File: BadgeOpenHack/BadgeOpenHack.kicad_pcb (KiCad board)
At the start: 2 copper layers, 38.1 x 48.2 mm, 27 parts, among them J1 Conn_01x04_Male, J2 USB_B_Micro, SW1 RST, U1 ATSAMD11C14A-SS, U2 AP2112K-3.3

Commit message: remove logos inncesary
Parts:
- removed the G*** at (180.0, 101.0)
- removed the G*** at (189.5, 95.5)

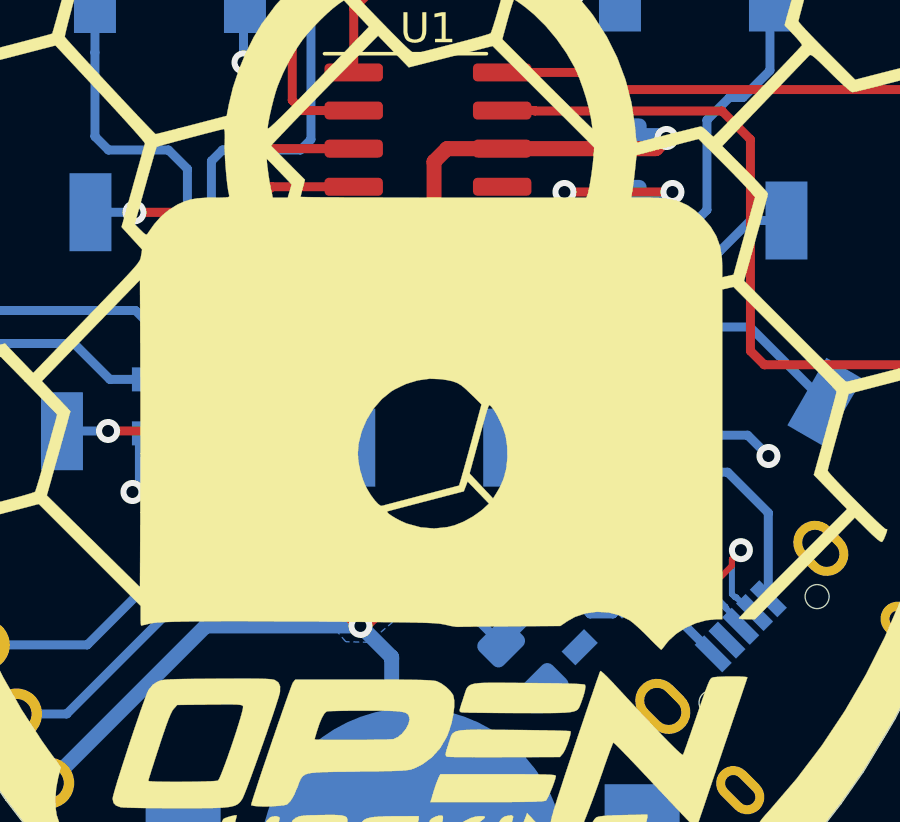
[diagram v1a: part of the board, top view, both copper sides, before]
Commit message: Fix logos and vias
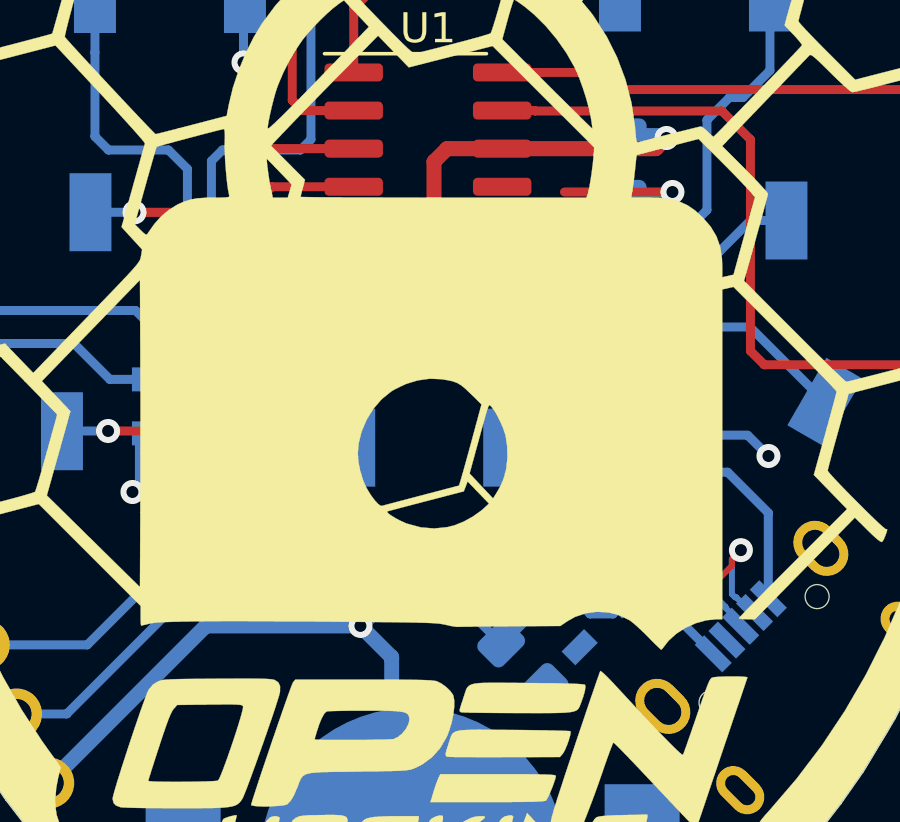
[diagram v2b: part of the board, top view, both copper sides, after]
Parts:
- removed REF**: OSHW-Logo2_7.3x6mm_SilkScreen, Symbol:OSHW-Logo2_7.3x6mm_SilkScreen
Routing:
- net +3V3: track 61.3 -> 63.7 mm
- net GND: vias 9 -> 8
- removed copper zone on B.Cu, net +3V3

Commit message: update pcb
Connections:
- BT1 pad 1: +3V3 -> GND
- BT1 pad 2: GND -> +3V3
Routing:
- net +3V3: track 63.7 -> 84.4 mm
- net GND: track 22.5 -> 28.8 mm, vias 8 -> 9
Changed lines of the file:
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@@
     (thickness 1.6)
     (drawings 60)
-    (tracks 275)
+    (tracks 299)
     (zones 0)
     (modules 24)
@@
     )
     (pad 1 smd circle (at 0 0) (size 10.2 10.2) (layers B.Cu B.Paste B.Mask)
-      (net 1 +3V3))
-    (pad 2 smd rect (at -7.65 0) (size 2.5 5.1) (layers B.Cu B.Paste B.Mask)
       (net 2 GND))
+    (pad 2 smd rect (at -7.65 0) (size 2.5 5.1) (layers B.Cu B.Paste B.Mask)
+      (net 1 +3V3))
     (pad 2 smd rect (at 7.65 0) (size 2.5 5.1) (layers B.Cu B.Paste B.Mask)
-      (net 2 GND))
+      (net 1 +3V3))
     (model ${KIPRJMOD}/BadgeOpenHack.pretty/3D/cr2430.step
       (offset (xyz 0 0 2))
       (scale (xyz 0.5 0.5 0.5))
-      (rotate (xyz 0 0 90))
+      (rotate (xyz 0 0 -90))
     )
   )
@@
   (gr_line (start 168.78 84.81) (end 168.78 98.22) (layer Edge.Cuts) (width 0.05))
   (gr_line (start 149.81 75.64) (end 168.78 84.81) (layer Edge.Cuts) (width 0.05))
-  (segment (start 148.640051 115.590051) (end 149.34 116.29) (width 0.5) (layer B.Cu) (net 1))
-  (segment (start 148.640051 109.549949) (end 148.640051 115.590051) (width 0.5) (layer B.Cu) (net 1))
   (via (at 147.6 108.464) (size 0.8) (drill 0.4) (layers F.Cu B.Cu) (net 1))
-  (segment (start 148.640051 109.504051) (end 147.6 108.464) (width 0.5) (layer B.Cu) (net 1))
-  (segment (start 148.640051 109.549949) (end 148.640051 109.504051) (width 0.5) (layer B.Cu) (net 1))
   (via (at 147.686 107.044) (size 0.8) (drill 0.4) (layers F.Cu B.Cu) (net 1))
   (via (at 148.406 107.734) (size 0.8) (drill 0.4) (layers F.Cu B.Cu) (net 1))
@@
   (segment (start 147.686 107.699685) (end 147.780315 107.794) (width 0.5) (layer B.Cu) (net 1))
   (segment (start 147.686 107.044) (end 147.686 107.699685) (width 0.5) (layer B.Cu) (net 1))
+  (segment (start 139.800286 116.29) (end 137.210351 113.700065) (width 0.5) (layer B.Cu) (net 1))
+  (segment (start 141.69 116.29) (end 139.800286 116.29) (width 0.5) (layer B.Cu) (net 1))
+  (segment (start 142.54703 119.947031) (end 141.69 119.090001) (width 0.5) (layer B.Cu) (net 1))
+  (segment (start 141.69 119.090001) (end 141.69 116.29) (width 0.5) (layer B.Cu) (net 1))
+  (segment (start 144.331922 121.029341) (end 143.461727 120.540468) (width 0.5) (layer B.Cu) (net 1))
+  (segment (start 146.044241 121.880759) (end 145.252581 121.519053) (width 0.5) (layer B.Cu) (net 1))
+  (segment (start 149.240793 123.075) (end 147.581646 122.517183) (width 0.5) (layer B.Cu) (net 1))
+  (segment (start 152.474774 122.250226) (end 151.152193 122.775715) (width 0.5) (layer B.Cu) (net 1))
+  (segment (start 145.252581 121.519053) (end 144.331922 121.029341) (width 0.5) (layer B.Cu) (net 1))
+  (segment (start 155.399843 120.913483) (end 155.136151 121.049874) (width 0.5) (layer B.Cu) (net 1))
+  (segment (start 152.664106 122.175) (end 152.55 122.175) (width 0.5) (layer B.Cu) (net 1))
+  (segment (start 146.244241 121.880759) (end 146.044241 121.880759) (width 0.5) (layer B.Cu) (net 1))
+  (segment (start 155.136151 121.049874) (end 153.359645 121.898648) (width 0.5) (layer B.Cu) (net 1))
+  (segment (start 151.152193 122.775715) (end 150.225557 123.075) (width 0.5) (layer B.Cu) (net 1))
+  (segment (start 146.410144 122.046663) (end 146.244241 121.880759) (width 0.5) (layer B.Cu) (net 1))
+  (segment (start 156.99 116.29) (end 156.99 119.634999) (width 0.5) (layer B.Cu) (net 1))
+  (segment (start 153.359645 121.898648) (end 152.664106 122.175) (width 0.5) (layer B.Cu) (net 1))
+  (segment (start 156.230972 120.394027) (end 155.399843 120.913483) (width 0.5) (layer B.Cu) (net 1))
+  (segment (start 143.461727 120.540468) (end 142.54703 119.947031) (width 0.5) (layer B.Cu) (net 1))
+  (segment (start 150.225557 123.075) (end 149.240793 123.075) (width 0.5) (layer B.Cu) (net 1))
+  (segment (start 156.99 119.634999) (end 156.230972 120.394027) (width 0.5) (layer B.Cu) (net 1))
+  (segment (start 147.581646 122.517183) (end 146.410144 122.046663) (width 0.5) (layer B.Cu) (net 1))
+  (segment (start 152.55 122.175) (end 152.474774 122.250226) (width 0.5) (layer B.Cu) (net 1))
+  (segment (start 146.410144 122.046662) (end 146.244241 121.880759) (width 0.5) (layer B.Cu) (net 1))
+  (segment (start 146.410144 122.046663) (end 146.410144 122.046662) (width 0.5) (layer B.Cu) (net 1))
   (segment (start 156.305216 106.434784) (end 157.844784 106.434784) (width 0.3) (layer B.Cu) (net 2))
   (segment (start 155.792817 106.947183) (end 156.305216 106.434784) (width 0.3) (layer B.Cu) (net 2))
@@
   (segment (start 155.038 98.6) (end 155.336 98.898) (width 0.3) (layer B.Cu) (net 2))
   (segment (start 153.16 98.6) (end 155.038 98.6) (width 0.3) (layer B.Cu) (net 2))
+  (via (at 149.25 110.025) (size 0.8) (drill 0.4) (layers F.Cu B.Cu) (net 2))
+  (segment (start 149.34 110.115) (end 149.25 110.025) (width 0.3) (layer B.Cu) (net 2))
+  (segment (start 149.34 116.29) (end 149.34 110.115) (width 0.3) (layer B.Cu) (net 2))
   (segment (start 133.2 99.05) (end 138.05 99.05) (width 0.3) (layer B.Cu) (net 3))
   (segment (start 138.05 99.05) (end 139.246 100.246) (width 0.3) (layer B.Cu) (net 3))
